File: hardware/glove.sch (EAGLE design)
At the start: 84 parts, among them J1 TC2030-JLINK-NL, J2 MICRO_USB_B_JST_MC5BR3-M404-4S, P1 DMP1045U, U1 NRF51822QF, U2 BNO055, U3 AT42QT1070, U4 MCP73831, U5 LP3855EMP-ADJ, X1 ABS05-32.768KHZ-9-T

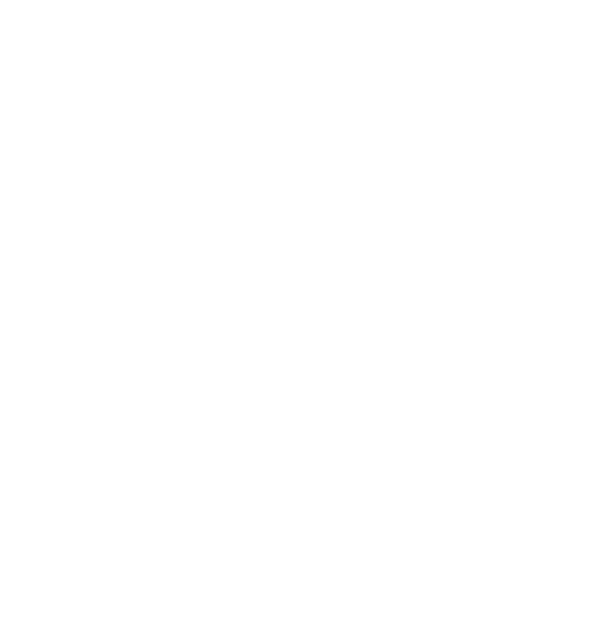
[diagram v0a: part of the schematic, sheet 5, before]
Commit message: Silkscreen/SPI LEDs
Cleaned up silk screen layer.
Added SPI connectors to schematic - still need to route.
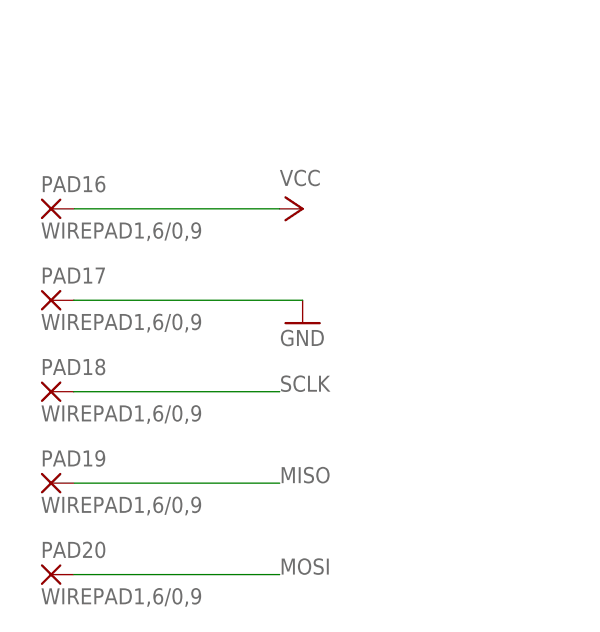
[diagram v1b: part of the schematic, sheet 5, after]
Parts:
- added PAD16, PAD17, PAD18, PAD19, PAD20: WIREPAD1,6/0,9, wirepad:WIREPAD1,6/0,9
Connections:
- new net MISO: PAD19.P, U1.P00/AREF0
- new net MOSI: PAD20.P, U1.P30
- new net SCLK: PAD18.P, U1.P06/AIN7/AREF1
- net GND: now also PAD17.P
- net VCC: now also PAD16.P
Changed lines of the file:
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@@
 <?xml version="1.0" encoding="utf-8"?>
 <!DOCTYPE eagle SYSTEM "eagle.dtd">
-<eagle version="6.6.0">
+<eagle version="7.7.0">
 <drawing>
 <settings>
@@
 <part name="P1" library="load_balance" deviceset="DMP1045U" device=""/>
 <part name="D1" library="load_balance" deviceset="B130LAW" device=""/>
+<part name="PAD16" library="wirepad" deviceset="WIREPAD" device="1,6/0,9" value="WIREPAD1,6/0,9"/>
+<part name="PAD17" library="wirepad" deviceset="WIREPAD" device="1,6/0,9" value="WIREPAD1,6/0,9"/>
+<part name="PAD18" library="wirepad" deviceset="WIREPAD" device="1,6/0,9" value="WIREPAD1,6/0,9"/>
+<part name="PAD19" library="wirepad" deviceset="WIREPAD" device="1,6/0,9" value="WIREPAD1,6/0,9"/>
+<part name="PAD20" library="wirepad" deviceset="WIREPAD" device="1,6/0,9" value="WIREPAD1,6/0,9"/>
+<part name="P+12" library="supply1" deviceset="VCC" device=""/>
+<part name="GND26" library="supply1" deviceset="GND" device=""/>
 </parts>
 <sheets>
@@
 <pinref part="U1" gate="G$1" pin="P05/AIN6"/>
 <wire x1="-22.86" y1="10.16" x2="-43.18" y2="10.16" width="0.1524" layer="91"/>
-<wire x1="-43.18" y1="10.16" x2="-43.18" y2="22.86" width="0.1524" layer="91"/>
-<label x="-43.18" y="22.86" size="1.778" layer="95"/>
+<wire x1="-43.18" y1="10.16" x2="-43.18" y2="15.24" width="0.1524" layer="91"/>
+<label x="-43.18" y="15.24" size="1.778" layer="95"/>
 </segment>
 </net>
@@
 <wire x1="22.86" y1="27.94" x2="30.48" y2="27.94" width="0.1524" layer="91"/>
 <label x="30.48" y="27.94" size="1.778" layer="95"/>
+</segment>
+</net>
+<net name="MISO" class="0">
+<segment>
+<pinref part="U1" gate="G$1" pin="P00/AREF0"/>
+<wire x1="-22.86" y1="22.86" x2="-43.18" y2="22.86" width="0.1524" layer="91"/>
+<label x="-43.18" y="22.86" size="1.778" layer="95"/>
+</segment>
+</net>
+<net name="MOSI" class="0">
+<segment>
+<pinref part="U1" gate="G$1" pin="P30"/>
+<wire x1="22.86" y1="-10.16" x2="30.48" y2="-10.16" width="0.1524" layer="91"/>
+<label x="25.4" y="-10.16" size="1.778" layer="95"/>
+</segment>
+</net>
+<net name="SCLK" class="0">
+<segment>
+<pinref part="U1" gate="G$1" pin="P06/AIN7/AREF1"/>
+<wire x1="-22.86" y1="7.62" x2="-33.02" y2="7.62" width="0.1524" layer="91"/>
+<label x="-33.02" y="7.62" size="1.778" layer="95"/>
 </segment>
 </net>
@@
 <instance part="GND24" gate="1" x="220.98" y="12.7"/>
 <instance part="P+11" gate="VCC" x="154.94" y="50.8"/>
+<instance part="PAD16" gate="G$1" x="-5.08" y="45.72"/>
+<instance part="PAD17" gate="G$1" x="-5.08" y="35.56"/>
+<instance part="PAD18" gate="G$1" x="-5.08" y="25.4"/>
+<instance part="PAD19" gate="G$1" x="-5.08" y="15.24"/>
+<instance part="PAD20" gate="G$1" x="-5.08" y="5.08"/>
+<instance part="P+12" gate="VCC" x="22.86" y="45.72" rot="R270"/>
+<instance part="GND26" gate="1" x="22.86" y="33.02"/>
 </instances>
 <busses>
@@
 <wire x1="154.94" y1="40.64" x2="190.5" y2="40.64" width="0.1524" layer="91"/>
 </segment>
+<segment>
+<pinref part="PAD16" gate="G$1" pin="P"/>
+<pinref part="P+12" gate="VCC" pin="VCC"/>
+<wire x1="-2.54" y1="45.72" x2="20.32" y2="45.72" width="0.1524" layer="91"/>
+</segment>
 </net>
 <net name="GND" class="0">
@@
 <wire x1="220.98" y1="20.32" x2="220.98" y2="15.24" width="0.1524" layer="91"/>
 <pinref part="GND24" gate="1" pin="GND"/>
+</segment>
+<segment>
+<pinref part="GND26" gate="1" pin="GND"/>
+<pinref part="PAD17" gate="G$1" pin="P"/>
+<wire x1="22.86" y1="35.56" x2="-2.54" y2="35.56" width="0.1524" layer="91"/>
 </segment>
 </net>
@@
 </segment>
 </net>
+<net name="SCLK" class="0">
+<segment>
+<pinref part="PAD18" gate="G$1" pin="P"/>
+<wire x1="-2.54" y1="25.4" x2="20.32" y2="25.4" width="0.1524" layer="91"/>
+<label x="20.32" y="25.4" size="1.778" layer="95"/>
+</segment>
+</net>
+<net name="MISO" class="0">
+<segment>
+<pinref part="PAD19" gate="G$1" pin="P"/>
+<wire x1="-2.54" y1="15.24" x2="20.32" y2="15.24" width="0.1524" layer="91"/>
+<label x="20.32" y="15.24" size="1.778" layer="95"/>
+</segment>
+</net>
+<net name="MOSI" class="0">
+<segment>
+<pinref part="PAD20" gate="G$1" pin="P"/>
+<wire x1="-2.54" y1="5.08" x2="20.32" y2="5.08" width="0.1524" layer="91"/>
+<label x="20.32" y="5.08" size="1.778" layer="95"/>
+</segment>
+</net>

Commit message: Adjusted Silkscreen
Named and adjusted pads and added slikscreen text
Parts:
- renumbered LED12 to LED1, LED13 to LED2, LED14 to LED3, LED15 to LED4, PAD1 to H+, PAD10 to F3+, PAD11 to F3-, PAD12 to T3, PAD13 to T2, PAD14 to T1, PAD15 to T0, PAD16 to SPI+, PAD17 to SPI-, PAD18 to SCLK, PAD19 to MISO, PAD2 to H-, PAD20 to MOSI, PAD3 to H-OUT, PAD4 to F0+, PAD5 to F0-, PAD6 to F1+, PAD7 to F1-, PAD8 to F2+, PAD9 to F2-
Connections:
- net N$31: now also R12.2; no longer R11.2
- net N$32: now also R12.1; no longer R11.1
- net N$33: now also R11.2; no longer R9.2
- net N$34: now also R11.1; no longer R9.1
- net N$35: now also R10.2; no longer R12.2
- net N$36: now also R10.1; no longer R12.1
- net N$37: now also R9.2; no longer R10.2
- net N$39: now also R9.1; no longer R10.1

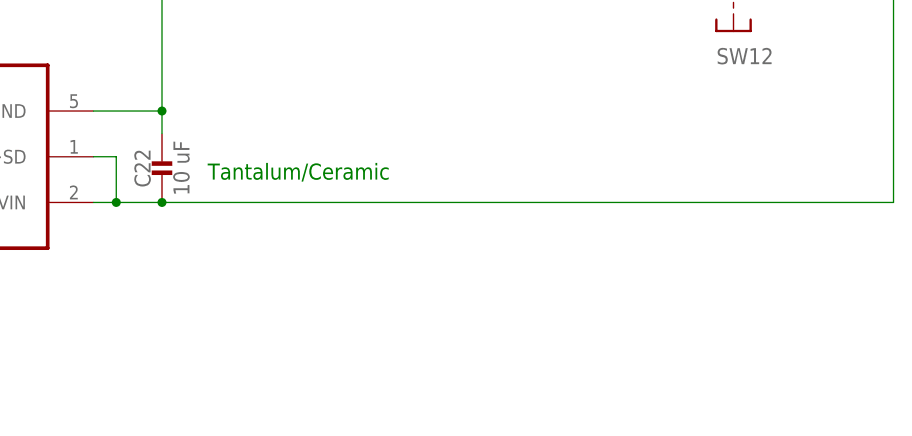
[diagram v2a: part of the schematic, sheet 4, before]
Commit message: Moved some parts slightly and ADDED PWR LED
Possible issues with bus routing
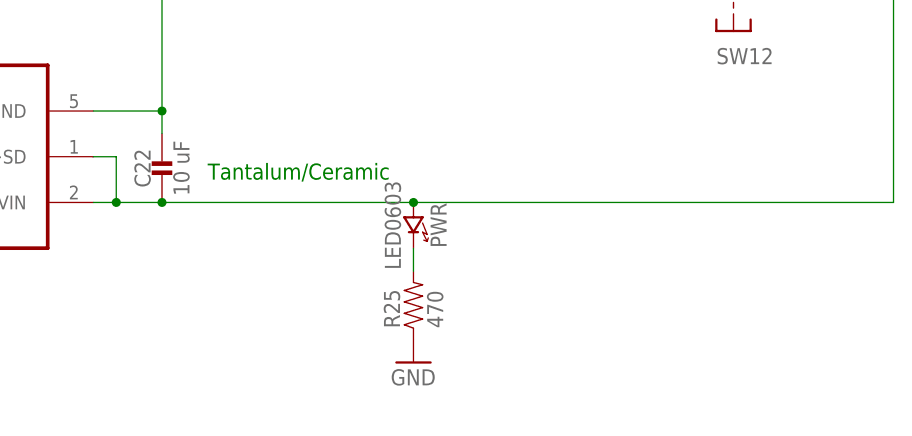
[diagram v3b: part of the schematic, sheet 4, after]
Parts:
- added PWR: LED0603, leds:LED0603
- added R25: 470, passives:RESISTOR0603_RES
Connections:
- new net N$17: PWR.CATHODE, R25.2
- net GND: now also R25.1
- net N$5: now also PWR.ANODE
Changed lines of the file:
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@@
 <part name="P+12" library="supply1" deviceset="VCC" device=""/>
 <part name="GND26" library="supply1" deviceset="GND" device=""/>
+<part name="R25" library="passives" deviceset="RESISTOR" device="0603_RES" value="470"/>
+<part name="PWR" library="leds" deviceset="LED" device="0603"/>
+<part name="GND27" library="supply1" deviceset="GND" device=""/>
 </parts>
 <sheets>
@@
 <instance part="P1" gate="G$1" x="60.96" y="25.4" rot="MR270"/>
 <instance part="D1" gate="G$1" x="83.82" y="17.78" rot="R270"/>
+<instance part="R25" gate="G$1" x="83.82" y="-27.94" rot="R90"/>
+<instance part="PWR" gate="G$1" x="83.82" y="-20.32" rot="R270"/>
+<instance part="GND27" gate="1" x="83.82" y="-35.56"/>
 </instances>
 <busses>
@@
 <junction x="101.6" y="33.02"/>
 </segment>
+<segment>
+<pinref part="R25" gate="G$1" pin="1"/>
+<pinref part="GND27" gate="1" pin="GND"/>
+</segment>
 </net>
 <net name="N$4" class="0">
@@
 <pinref part="U5" gate="A" pin="VIN"/>
 <wire x1="137.16" y1="12.7" x2="137.16" y2="-17.78" width="0.1524" layer="91"/>
-<wire x1="137.16" y1="-17.78" x2="55.88" y2="-17.78" width="0.1524" layer="91"/>
+<wire x1="137.16" y1="-17.78" x2="83.82" y2="-17.78" width="0.1524" layer="91"/>
 <pinref part="C22" gate="G$1" pin="2"/>
+<wire x1="83.82" y1="-17.78" x2="55.88" y2="-17.78" width="0.1524" layer="91"/>
 <wire x1="55.88" y1="-17.78" x2="50.8" y2="-17.78" width="0.1524" layer="91"/>
 <junction x="55.88" y="-17.78"/>
@@
 <wire x1="50.8" y1="-12.7" x2="50.8" y2="-17.78" width="0.1524" layer="91"/>
 <junction x="50.8" y="-17.78"/>
+<pinref part="PWR" gate="G$1" pin="ANODE"/>
+<junction x="83.82" y="-17.78"/>
 </segment>
 </net>
@@
 </segment>
 </net>
+<net name="N$17" class="0">
+<segment>
+<pinref part="PWR" gate="G$1" pin="CATHODE"/>
+<pinref part="R25" gate="G$1" pin="2"/>
+<wire x1="83.82" y1="-22.86" x2="83.82" y2="-25.4" width="0.1524" layer="91"/>
+</segment>
+</net>

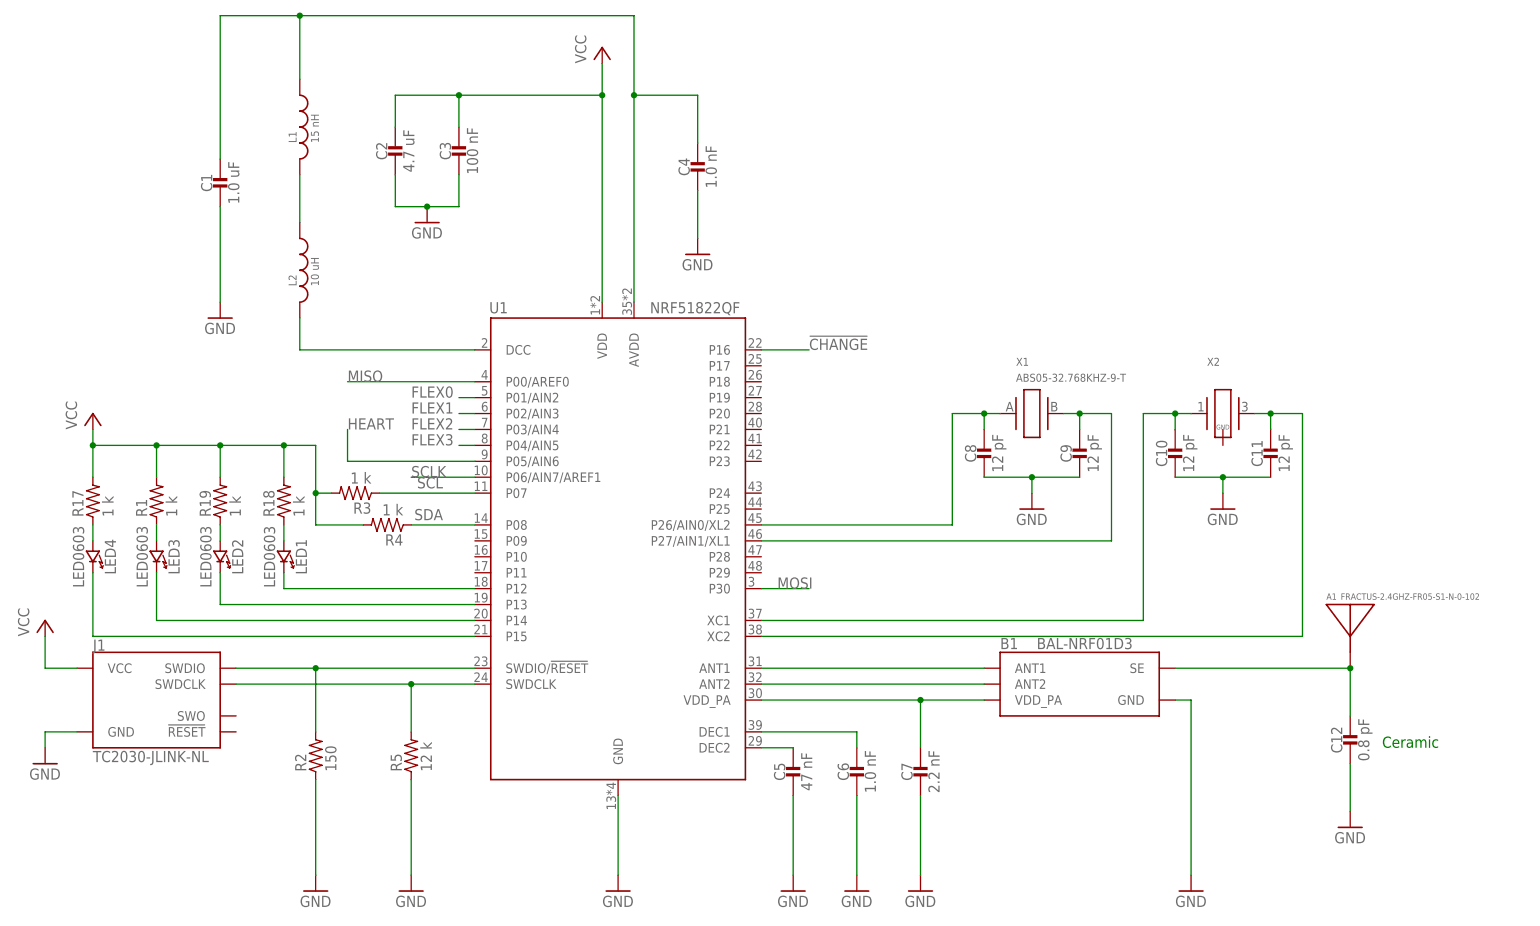
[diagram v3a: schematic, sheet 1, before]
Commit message: Renamed Parts/Updated BOM
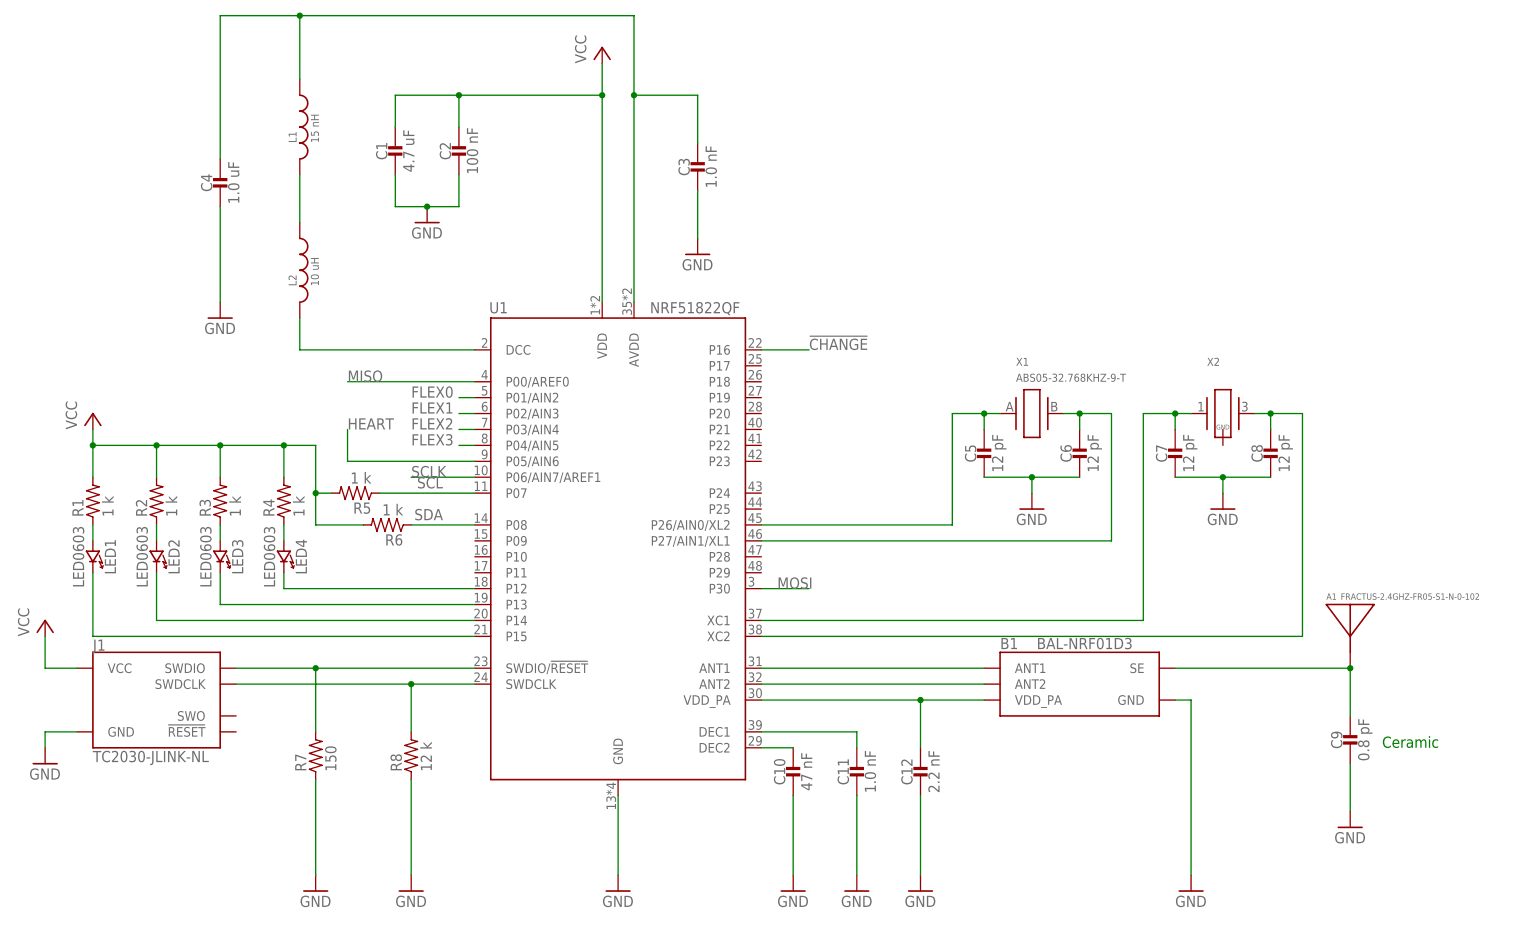
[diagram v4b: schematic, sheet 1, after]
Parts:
- C1: value 1.0 uF -> 4.7 uF
- C10: value 12 pF -> 47 nF
- C11: value 12 pF -> 1.0 nF
- C12: value 0.8 pF -> 2.2 nF
- C13: value 100 nF -> 6.8 nF
- C14: value 6.8 nF -> 120 nF
- C15: value 120 nF -> 100 nF
- C18: value 4.7 uF -> 1uF
- C19: value 8 nF -> 4.7 uF
- C2: value 4.7 uF -> 100 nF; device passives:CAPACITOR0603_CAP -> passives:CAPACITOR0402_CAP
- C20: value 10 uF -> 4.7 uF
- C21: value 4.7 uF -> 8 nF
- C23: value 1uF -> 10 uF
- C3: value 100 nF -> 1.0 nF
- C4: value 1.0 nF -> 1.0 uF; device passives:CAPACITOR0402_CAP -> passives:CAPACITOR0603_CAP
- C5: value 47 nF -> 12 pF
- C6: value 1.0 nF -> 12 pF
- C7: value 2.2 nF -> 12 pF
- C9: value 12 pF -> 0.8 pF
- R10, R11: value 10 k -> 47 k
- R13: value 470 -> 10 k
- R14: value 250 -> 10 k
- R15: value 440 -> 10 k
- R16: value 2 k -> 100k
- R17: value 1 k -> 470
- R18: value 1 k -> 2 k
- R19: value 1 k -> 250
- R2: value 150 -> 1 k
- R20: value (none) -> 440
- R21: value (none) -> 470
- R24: value 100k -> (none)
- R25: value 470 -> (none)
- R5: value 12 k -> 1 k
- R6: value 10 k -> 1 k
- R7: value 47 k -> 150
- R8: value 47 k -> 12 k
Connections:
- net !CHANGE: now also R11.1; no longer R8.1
- net FLEX0: now also R22.1; no longer R20.1
- net FLEX1: now also R23.1; no longer R21.1
- net FLEX2: now also R24.1; no longer R22.1
- net FLEX3: now also R25.1; no longer R23.1
- net GND: now also C18.1, C19.2, C23.2, R18.1, R19.2, R21.1, R24.2, R25.2, R7.1, R8.1; no longer C18.2, C21.2, C23.1, R14.2, R2.1, R20.2, R21.2, R24.1, R25.1, R5.1
- net N$1: now also C18.2; no longer C23.2
- net N$10: now also LED1.CATHODE; no longer LED4.CATHODE
- net N$11: now also LED1.ANODE, R1.1; no longer LED4.ANODE, R17.1
- net N$12: now also LED4.CATHODE; no longer LED1.CATHODE
- net N$13: now also LED4.ANODE, R4.1; no longer LED1.ANODE, R18.1
- net N$16: now also C3.1; no longer C1.1
- net N$17: now also R21.2; no longer R25.2
- net N$18: now also R9.1; no longer R6.1
- net N$19: now also R7.2; no longer R2.2
- net N$2: now also R17.1; no longer R13.1
- net N$20: now also C8.1; no longer C11.1
- net N$23: now also C12.1; no longer C7.1
- net N$24: now also C9.1; no longer C12.1
- net N$25: now also C10.1; no longer C5.1
- net N$26: now also C11.1; no longer C6.1
- net N$27: now also C5.1; no longer C8.1
- net N$28: now also C6.1; no longer C9.1
- net N$29: now also C7.1; no longer C10.1
- net N$30: now also R8.2; no longer R5.2
- net N$33: now also R13.2; no longer R11.2
- net N$34: now also R13.1; no longer R11.1
- net N$35: now also R14.2; no longer R10.2
- net N$36: now also R14.1; no longer R10.1
- net N$37: now also R15.2; no longer R9.2
- net N$38: now also C19.1, R16.2, R17.2; no longer C18.1, R13.2, R24.2
- net N$39: now also R15.1; no longer R9.1
- net N$4: now also R18.2; no longer R16.2
- net N$40: now also R10.1; no longer R7.1
- net N$41: now also C20.1; no longer C21.1
- net N$42: now also LED3.ANODE, R3.1; no longer LED2.ANODE, R19.1
- net N$43: now also LED3.CATHODE; no longer LED2.CATHODE
- net N$6: now also LED2.CATHODE; no longer LED3.CATHODE
- net N$7: now also C21.1, R19.1, R20.2; no longer C19.1, R14.1, R15.2
- net N$8: now also LED2.ANODE, R2.1; no longer LED3.ANODE, R1.1
- net N$9: now also C16.1; no longer C13.1
- net SCL: now also R5.1; no longer R3.1
- net SDA: now also R6.1; no longer R4.1
- net VCC: now also C1.1, C13.1, C21.2, C23.1, R10.2, R11.2, R2.2, R20.1, R5.2, R9.2; no longer C16.1, C19.2, C20.1, C3.1, R15.1, R17.2, R18.2, R19.2, R7.2, R8.2
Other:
- note removed: "<1cm away from device"
- note removed: "Tantalum"
- note removed: "Tantalum/Ceramic"
- moved on the sheet: C1, C10, C11, C12, C13, C14, C15, C16, C18, C19, C2, C20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

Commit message: The board is done...hopefully
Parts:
- removed MISO: WIREPAD1,6/0,9, wirepad:WIREPAD1,6/0,9
- R21: value 470 -> 250
- R22, R23, R24, R25: value (none) -> 20k
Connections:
- removed net MISO: MISO.P, U1.P00/AREF0
- removed net N$5: C22.2, PWR.ANODE, SW11.O, SW12.O, U5.VIN, U5.~SD
- new net N$54: C22.2, SW11.O, SW12.O, U5.VIN, U5.~SD
- net MOSI: now also U1.P17; no longer U1.P30
- net SCLK: now also U1.P18; no longer U1.P06/AIN7/AREF1
- net SDA: now also R6.2, U1.P30; no longer R6.1, U1.P08
- net VCC: now also PWR.ANODE, R6.1; no longer R6.2
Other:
- moved on the sheet: MOSI, PWR, R21, R6
